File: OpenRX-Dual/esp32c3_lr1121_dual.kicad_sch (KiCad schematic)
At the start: 44 parts, among them T1 0900PC16J0042001E, U1 ESP32-C3FH4, U2 TLV75533PDQNR, U3 RFX2401C, U4 LR1121IMLTRT, U5 OW2EL89CENUXFMYLC-32M, X1 CJ17-400001010B20

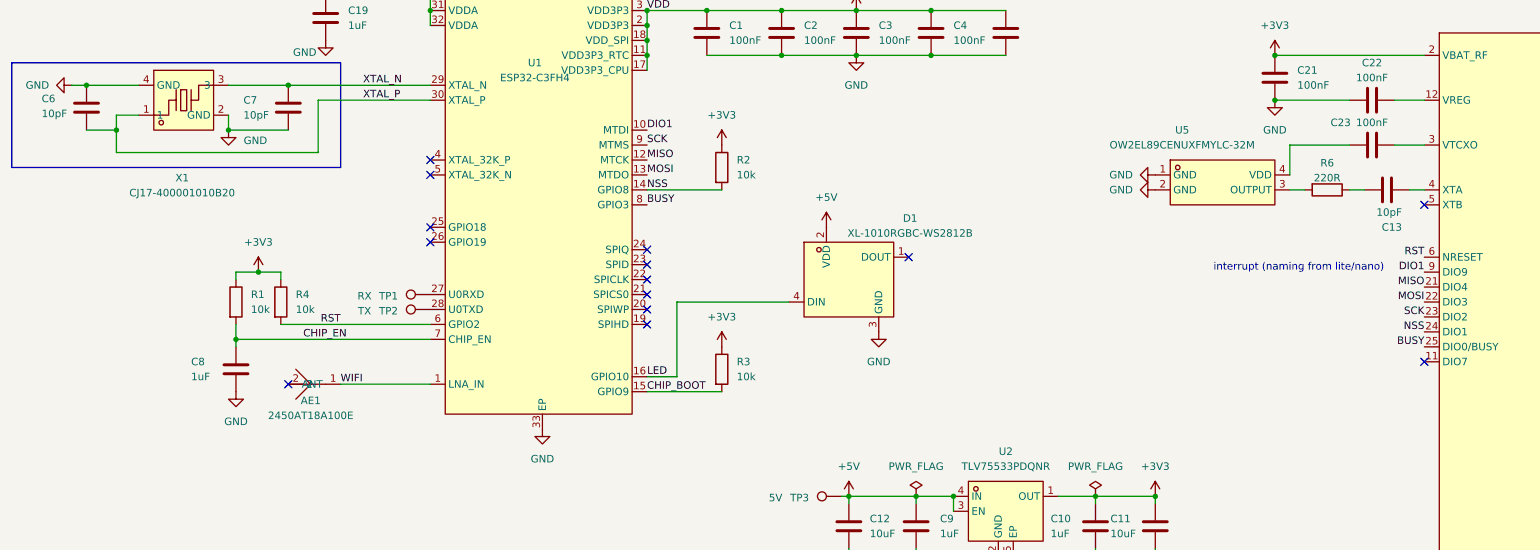
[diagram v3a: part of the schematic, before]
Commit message: Fix crystal load caps: 10pF → 18pF (C71153) on all 4 receivers
CJ17-400001010B20 crystal has CL=10pF. With 10pF load caps and
~2pF stray, effective load was only 7pF (30% low). Changed to 18pF
giving ~11pF effective load, matching the crystal spec.

C71153 = Samsung CL03C180JA3NNNC, 18pF C0G 25V 0201.
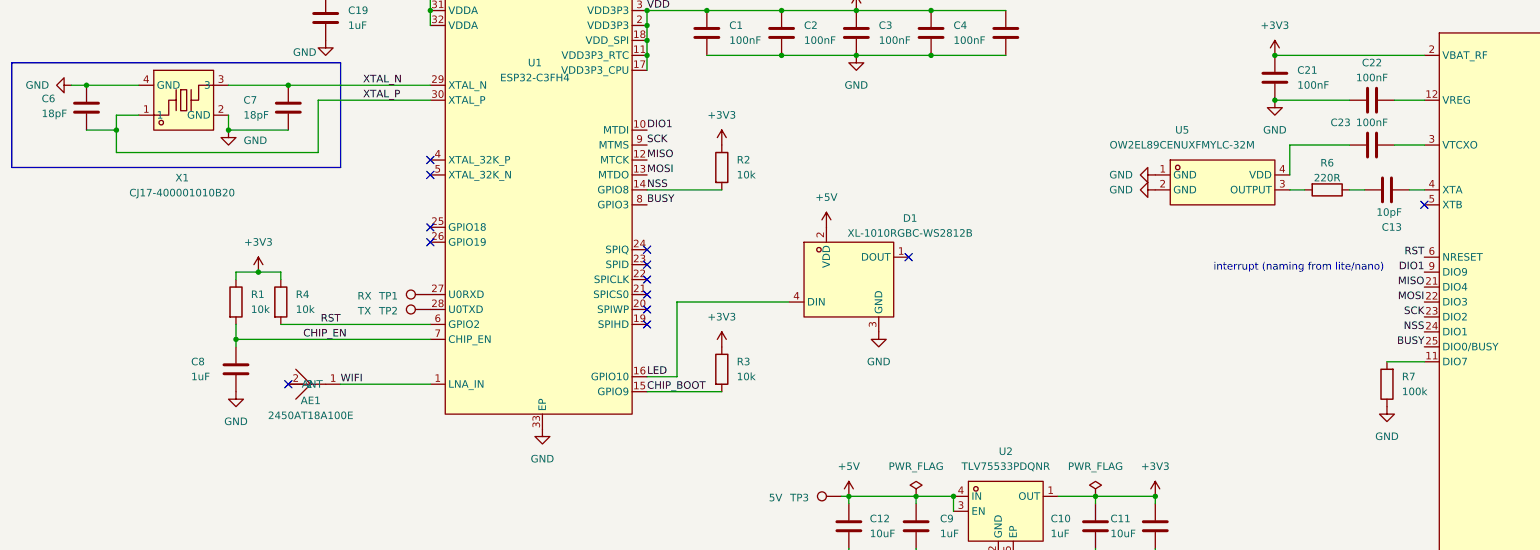
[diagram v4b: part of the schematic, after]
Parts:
- added R7: 100k, Resistor_SMD:R_0201_0603Metric, symbol Device:R
- C6, C7: value 10pF -> 18pF; LCSC C14854 -> C71153
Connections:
- net GND: now also R7.1
- net at U4.11 (DIO7): now also R7.2
- no-connect marks 22 -> 21
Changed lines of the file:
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@@
 	)
 	(no_connect
-		(at 266.7 88.9)
-	)
-	(no_connect
 		(at 309.88 67.31)
 	)
@@
 	(wire
 		(pts
+			(xy 260.35 88.9) (xy 266.7 88.9)
+		)
+		(stroke
+			(width 0)
+			(type default)
+		)
+	)
+	(wire
+		(pts
 			(xy 64.77 85.09) (xy 64.77 86.36)
 		)
@@
 	)
 	(symbol
+		(lib_id "power:GND")
+		(at 260.35 96.52 0)
+		(unit 1)
+		(body_style 1)
+		(exclude_from_sim no)
+		(in_bom yes)
+		(on_board yes)
+		(in_pos_files yes)
+		(dnp no)
+		(fields_autoplaced yes)
+		(property "Reference" "#PWR047"
+			(at 260.35 102.87 0)
+			(hide yes)
+			(show_name no)
+			(do_not_autoplace no)
+			(effects
+				(font
+					(size 1.27 1.27)
+				)
+			)
+		)
+		(property "Value" "GND"
+			(at 260.35 101.6 0)
+			(show_name no)
+			(do_not_autoplace no)
+			(effects
+				(font
+					(size 1.27 1.27)
+				)
+			)
+		)
+		(property "Footprint" ""
+			(at 260.35 96.52 0)
+			(hide yes)
+			(show_name no)
+			(do_not_autoplace no)
+			(effects
+				(font
+					(size 1.27 1.27)
+				)
+			)
+		)
+		(property "Datasheet" ""
+			(at 260.35 96.52 0)
+			(hide yes)
+			(show_name no)
+			(do_not_autoplace no)
+			(effects
+				(font
+					(size 1.27 1.27)
+				)
+			)
+		)
+		(property "Description" "Power symbol creates a global label with name \"GND\" , ground"
+			(at 260.35 96.52 0)
+			(hide yes)
+			(show_name no)
+			(do_not_autoplace no)
+			(effects
+				(font
+					(size 1.27 1.27)
+				)
+			)
+		)
+		(pin "1"
+		)
+		(instances
+			(project "OpenRX-Dual"
+				(path "/b1c2d3e4-f5a6-7890-bcde-f12345678901/f1e2d3c4-b5a6-7890-1234-567890fedcba"
+					(reference "#PWR047")
+					(unit 1)
+				)
+			)
+		)
+	)
+	(symbol
 		(lib_id "Device:C")
 		(at 73.66 45.72 0)
@@
 			)
 		)
-		(property "Value" "10pF"
+		(property "Value" "18pF"
 			(at 66.04 46.99 0)
 			(show_name no)
@@
 			)
 		)
-		(property "LCSC" "C14854"
+		(property "LCSC" "C71153"
 			(at 0 0 0)
 			(hide yes)
@@
 			)
 		)
-		(property "Value" "10pF"
+		(property "Value" "18pF"
 			(at 31.75 46.736 0)
 			(show_name no)
@@
 			)
 		)
-		(property "LCSC" "C14854"
+		(property "LCSC" "C71153"
 			(at 0 0 0)
 			(hide yes)
@@
 	)
 	(symbol
+		(lib_id "Device:R")
+		(at 260.35 92.71 180)
+		(unit 1)
+		(body_style 1)
+		(exclude_from_sim no)
+		(in_bom yes)
+		(on_board yes)
+		(in_pos_files yes)
+		(dnp no)
+		(fields_autoplaced yes)
+		(property "Reference" "R7"
+			(at 262.89 91.4399 0)
+			(show_name no)
+			(do_not_autoplace no)
+			(effects
+				(font
+					(size 1.27 1.27)
+				)
+				(justify right)
+			)
+		)
+		(property "Value" "100k"
+			(at 262.89 93.9799 0)
+			(show_name no)
+			(do_not_autoplace no)
+			(effects
+				(font
+					(size 1.27 1.27)
+				)
+				(justify right)
+			)
+		)
+		(property "Footprint" "Resistor_SMD:R_0201_0603Metric"
+			(at 262.128 92.71 90)
+			(hide yes)
+			(show_name no)
+			(do_not_autoplace no)
+			(effects
+				(font
+					(size 1.27 1.27)
+				)
+			)
+		)
+		(property "Datasheet" ""
+			(at 260.35 92.71 0)
+			(hide yes)
+			(show_name no)
+			(do_not_autoplace no)
+			(effects
+				(font
+					(size 1.27 1.27)
+				)
+			)
+		)
+		(property "Description" "Resistor"
+			(at 260.35 92.71 0)
+			(hide yes)
+			(show_name no)
+			(do_not_autoplace no)
+			(effects
+				(font
+					(size 1.27 1.27)
+				)
+			)
+		)
+		(property "LCSC" "C25741"
+			(at -62.23 31.75 0)
+			(hide yes)
+			(show_name no)
+			(do_not_autoplace no)
+			(effects
+				(font
+					(size 1.27 1.27)
+				)
+			)
+		)
+		(pin "2"
+		)
+		(pin "1"
+		)
+		(instances
+			(project "OpenRX-Dual"
+				(path "/b1c2d3e4-f5a6-7890-bcde-f12345678901/f1e2d3c4-b5a6-7890-1234-567890fedcba"
+					(reference "R7")
+					(unit 1)
+				)
+			)
+		)
+	)
+	(symbol
 		(lib_id "Connector:TestPoint")
 		(at 97.79 77.47 90)
@@
 		)
 		(property "LCSC" "C25092"
-			(at 189.23 382.27 0)
-			(hide yes)
-			(show_name no)
-			(do_not_autoplace no)
-			(effects
-				(font
-					(size 1.27 1.27)
-				)
-			)
-		)
-		(property "LCSC" "C25092"
 			(at 0 0 0)
-			(show_name no)
-			(do_not_autoplace no)
 			(hide yes)
-			(effects
-				(font
-					(size 1.27 1.27)
-				)
-			)
-		)
-		(property "LCSC" "C25092"
-			(at 0 0 0)
 			(show_name no)
 			(do_not_autoplace no)
-			(hide yes)
 			(effects
 				(font
